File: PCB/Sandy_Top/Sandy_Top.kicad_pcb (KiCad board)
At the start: 2 copper layers, 285 x 37 mm, 64 parts, among them J1 Conn_02x02_Top_Bottom, J2 Conn_02x02_Top_Bottom, J3 Conn_02x02_Top_Bottom

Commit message: キーの間からEXT端子が見えないように移動した
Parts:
- moved EXT_TC3 1.19 mm to (149.6, 21.1)
- moved EXT_TC7 1.19 mm to (280.6, 21.1)
- moved EXT_TC0 1.19 mm to (35.3, 21.1)
- moved EXT_TC2 1.19 mm to (92.5, 21.1)
- moved EXT_TC1 1.19 mm to (73.4, 21.1)
- moved EXT_TC4 1.19 mm to (166.3, 21.0)
- moved EXT_TC6 1.19 mm to (261.6, 21.1)
- moved EXT_TR5 1.19 mm to (54.4, 21.1)
- moved EXT_TR0 1.19 mm to (35.3, 33.0)
- moved EXT_TC5 1.19 mm to (223.5, 21.1)
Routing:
- net Top_col2: track 62.9 -> 61.7 mm
- net Top_col7: track 139.3 -> 140.0 mm
- net Top_col4: track 76.2 -> 75.5 mm

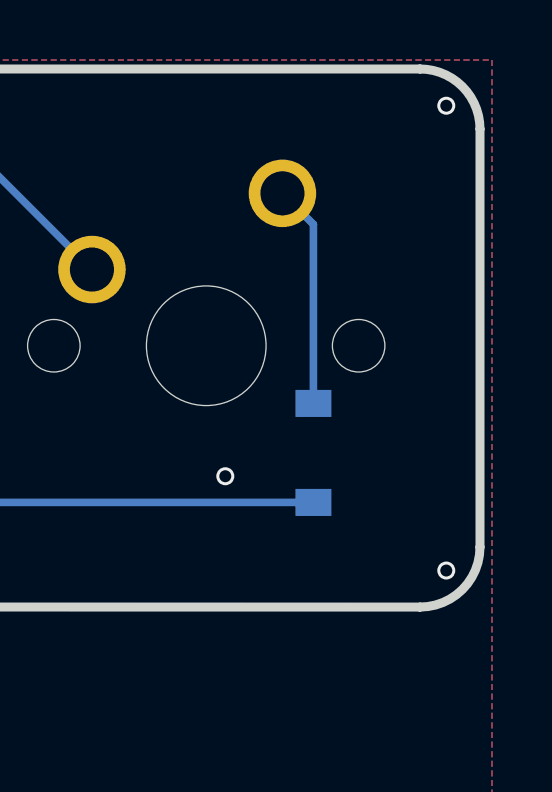
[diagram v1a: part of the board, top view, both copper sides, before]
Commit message: コネクタの接続先がわかるシルクを追加
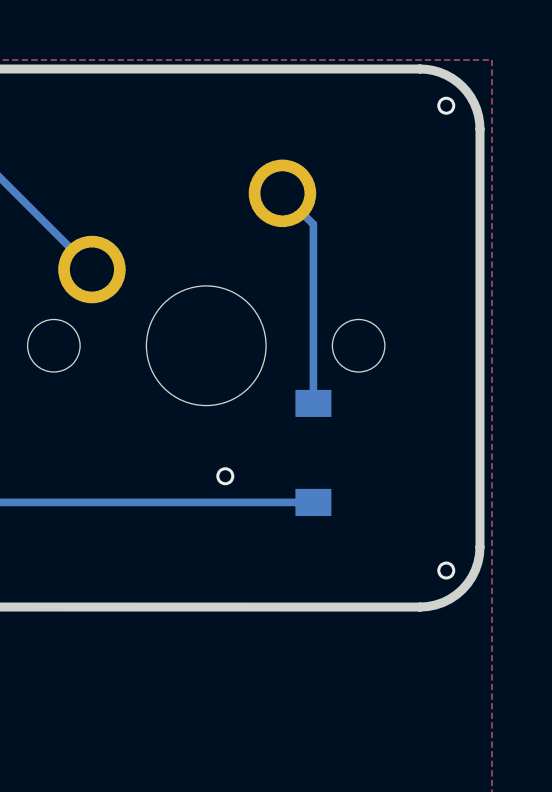
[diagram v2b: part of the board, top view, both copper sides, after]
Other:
- board text added: "Top 1"
- board text added: "Top 2"
- board text added: "Top 3"
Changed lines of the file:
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@@
     (fp_arc (start -140.510786 -0.814254) (mid -141.925 -1.40004) (end -142.510786 -2.814254) (layer "Edge.Cuts") (width 0.3))
     (fp_arc (start -39.470786 -0.82504) (mid -38.056572 -0.239254) (end -37.470786 1.17496) (layer "Edge.Cuts") (width 0.3))
-    (fp_arc (start 142.475 -2.814254) (mid 141.889203 -1.400035) (end 140.475 -0.814254) (layer "Edge.Cuts") (width 0.3))
+    (fp_arc (start 142.475 -2.814254) (mid 141.889197 -1.40007) (end 140.475 -0.814254) (layer "Edge.Cuts") (width 0.3))
     (fp_arc (start -35.470786 18.24996) (mid -36.885 17.664174) (end -37.470786 16.24996) (layer "Edge.Cuts") (width 0.3))
-    (fp_arc (start 140.475 -18.75004) (mid 141.889257 -18.164285) (end 142.475 -16.75004) (layer "Edge.Cuts") (width 0.3))
+    (fp_arc (start 140.475 -18.75004) (mid 141.889222 -18.164279) (end 142.475 -16.75004) (layer "Edge.Cuts") (width 0.3))
     (fp_arc (start -142.525 -16.75004) (mid -141.939214 -18.164254) (end -140.525 -18.75004) (layer "Edge.Cuts") (width 0.3))
     (fp_circle (center -47.625 -14.50004) (end -45.425 -14.50004) (layer "Edge.Cuts") (width 0.15) (fill none))
@@
     (property "Sheetname" "")
     (attr exclude_from_pos_files)
-    (fp_text reference "EXT_TR1" (at 0 1.998) (layer "B.SilkS")
+    (fp_text reference "EXT_TR1" (at -2.111375 -2.286) (layer "B.SilkS")
       (effects (font (size 1 1) (thickness 0.15)) (justify mirror))
     )
@@
     (property "Sheetname" "")
     (attr exclude_from_pos_files)
-    (fp_text reference "EXT_TR6" (at 0 -2.38125) (layer "B.SilkS")
+    (fp_text reference "EXT_TR6" (at 2.19075 -2.286) (layer "B.SilkS")
       (effects (font (size 1 1) (thickness 0.15)) (justify mirror))
     )
@@
     )
   )
+  (gr_text "Top 1" (at 172.26781 31.765905 90) (layer "B.SilkS")
+    (effects (font (size 1.2 1.2) (thickness 0.15)) (justify mirror))
+  )
+  (gr_text "Top 3" (at 153.21781 31.765905 90) (layer "B.SilkS")
+    (effects (font (size 1.2 1.2) (thickness 0.15)) (justify mirror))
+  )
+  (gr_text "Top 2" (at 131.78656 30.57528) (layer "B.SilkS")
+    (effects (font (size 1.2 1.2) (thickness 0.15)) (justify mirror))
+  )
   (gr_text "JLCJLCJLCJLC" (at 290.94931 34.242405) (layer "B.SilkS")

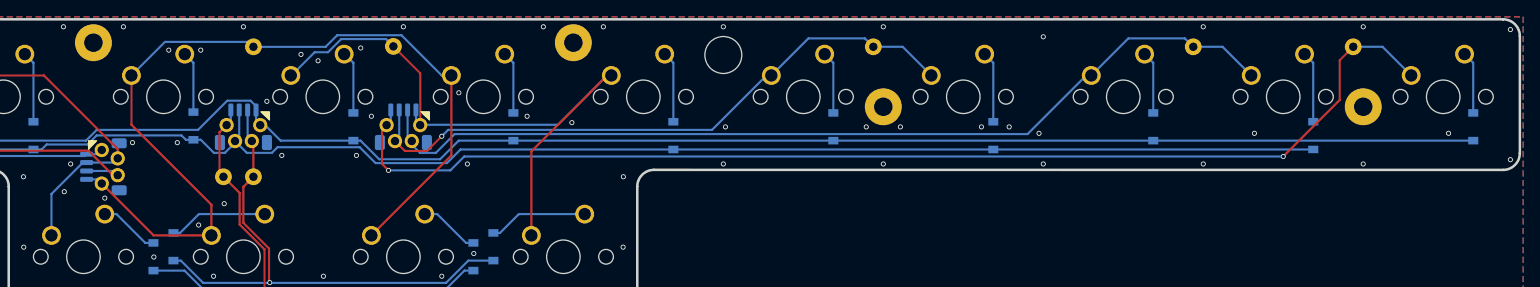
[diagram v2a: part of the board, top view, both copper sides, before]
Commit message: "Back Side"シルク位置調整
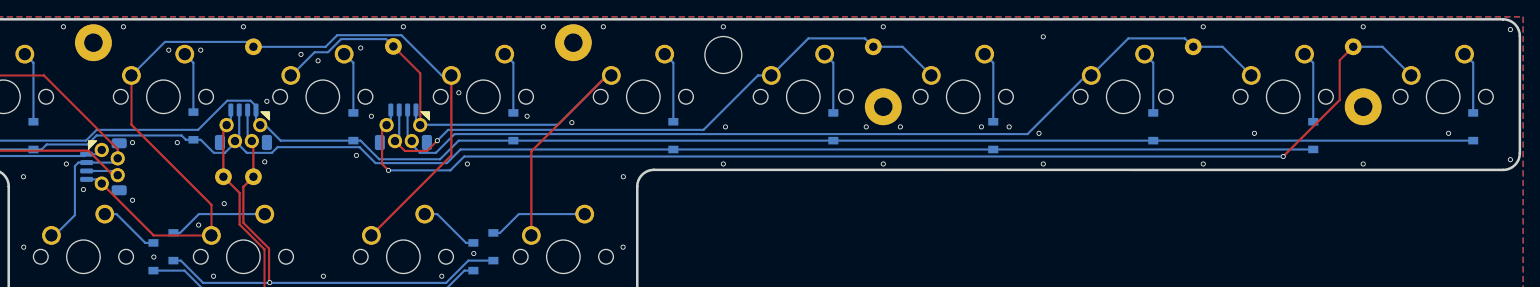
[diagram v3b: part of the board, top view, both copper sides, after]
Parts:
- removed G***: LOGO, Jones.local:Sandy_logo_w15
- renumbered J3 to J1, J1 to J3
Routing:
- net Top_col2: track 61.7 -> 62.2 mm

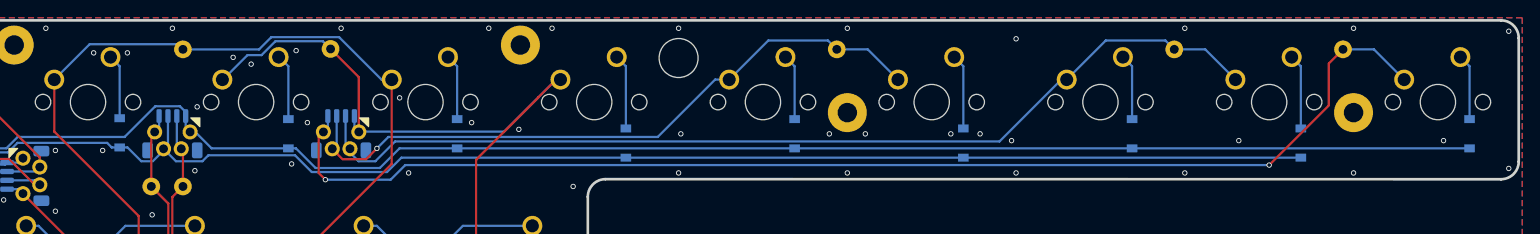
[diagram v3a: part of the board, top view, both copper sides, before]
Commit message: GNDベタ調整
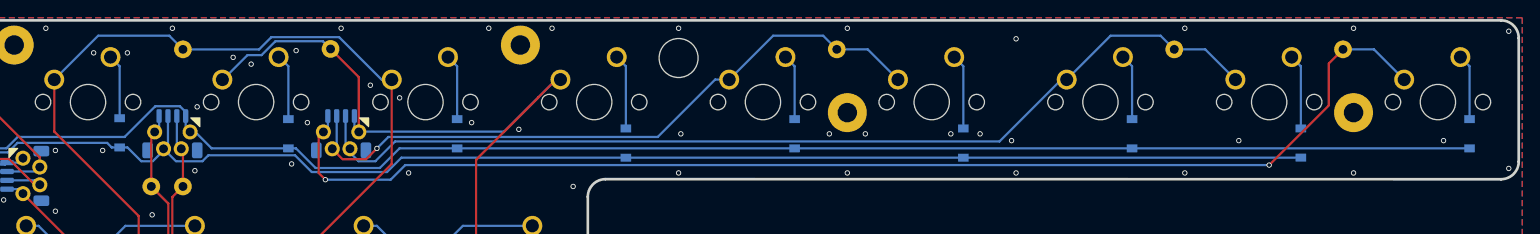
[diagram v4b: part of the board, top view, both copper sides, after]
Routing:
- net Top_col3: track 106.2 -> 107.0 mm
- net Top_GND: vias 78 -> 79
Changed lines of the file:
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@@
     (fp_arc (start -140.510786 -0.814254) (mid -141.925 -1.40004) (end -142.510786 -2.814254) (layer "Edge.Cuts") (width 0.3))
     (fp_arc (start -39.470786 -0.82504) (mid -38.056572 -0.239254) (end -37.470786 1.17496) (layer "Edge.Cuts") (width 0.3))
-    (fp_arc (start 142.475 -2.814254) (mid 141.889203 -1.400035) (end 140.475 -0.814254) (layer "Edge.Cuts") (width 0.3))
+    (fp_arc (start 142.475 -2.814254) (mid 141.889197 -1.40007) (end 140.475 -0.814254) (layer "Edge.Cuts") (width 0.3))
     (fp_arc (start -35.470786 18.24996) (mid -36.885 17.664174) (end -37.470786 16.24996) (layer "Edge.Cuts") (width 0.3))
-    (fp_arc (start 140.475 -18.75004) (mid 141.889257 -18.164285) (end 142.475 -16.75004) (layer "Edge.Cuts") (width 0.3))
+    (fp_arc (start 140.475 -18.75004) (mid 141.889222 -18.164279) (end 142.475 -16.75004) (layer "Edge.Cuts") (width 0.3))
     (fp_arc (start -142.525 -16.75004) (mid -141.939214 -18.164254) (end -140.525 -18.75004) (layer "Edge.Cuts") (width 0.3))
     (fp_circle (center -47.625 -14.50004) (end -45.425 -14.50004) (layer "Edge.Cuts") (width 0.15) (fill none))
@@
   (segment (start 172.069372 24.463405) (end 167.279172 19.673205) (width 0.254) (layer "B.Cu") (net 27))
   (segment (start 129.78656 36.83778) (end 131.08656 36.83778) (width 0.254) (layer "B.Cu") (net 27))
-  (segment (start 135.12031 24.463405) (end 139.11551 20.468205) (width 0.254) (layer "B.Cu") (net 27))
   (segment (start 131.08656 36.83778) (end 131.58656 37.33778) (width 0.254) (layer "B.Cu") (net 27))
   (segment (start 149.65531 21.059655) (end 149.645935 21.05028) (width 0.254) (layer "B.Cu") (net 27))
+  (segment (start 140.07331 19.510405) (end 148.10606 19.510405) (width 0.254) (layer "B.Cu") (net 27))
   (segment (start 173.22031 24.463405) (end 172.069372 24.463405) (width 0.254) (layer "B.Cu") (net 27))
+  (segment (start 148.10606 19.510405) (end 149.645935 21.05028) (width 0.254) (layer "B.Cu") (net 27))
   (segment (start 167.279172 19.673205) (end 159.62726 19.673205) (width 0.254) (layer "B.Cu") (net 27))
   (segment (start 159.62726 19.673205) (end 158.24081 21.059655) (width 0.254) (layer "B.Cu") (net 27))
-  (segment (start 149.06386 20.468205) (end 149.645935 21.05028) (width 0.254) (layer "B.Cu") (net 27))
-  (segment (start 139.11551 20.468205) (end 149.06386 20.468205) (width 0.254) (layer "B.Cu") (net 27))
   (segment (start 158.24081 21.059655) (end 149.65531 21.059655) (width 0.254) (layer "B.Cu") (net 27))
+  (segment (start 135.12031 24.463405) (end 140.07331 19.510405) (width 0.254) (layer "B.Cu") (net 27))
   (segment (start 169.50531 24.19403) (end 166.314685 21.003405) (width 0.254) (layer "F.Cu") (net 28))
   (segment (start 169.50531 30.37528) (end 169.50531 24.19403) (width 0.254) (layer "F.Cu") (net 28))
@@
   (segment (start 167.68551 33.45548) (end 170.324236 33.45548) (width 0.254) (layer "F.Cu") (net 29))
   (via (at 171.545498 32.234218) (size 0.6) (drill 0.4) (layers "F.Cu" "B.Cu") (net 29))
+  (segment (start 216.27331 19.510405) (end 211.32031 24.463405) (width 0.254) (layer "B.Cu") (net 29))
   (segment (start 172.839311 30.940405) (end 171.545498 32.234218) (width 0.254) (layer "B.Cu") (net 29))
   (segment (start 209.72932 24.463405) (end 203.25232 30.940405) (width 0.254) (layer "B.Cu") (net 29))
+  (segment (start 221.92481 19.510405) (end 216.27331 19.510405) (width 0.254) (layer "B.Cu") (net 29))
   (segment (start 167.00531 31.77528) (end 167.00531 28.57528) (width 0.254) (layer "B.Cu") (net 29))
   (segment (start 203.25232 30.940405) (end 172.839311 30.940405) (width 0.254) (layer "B.Cu") (net 29))
   (segment (start 211.32031 24.463405) (end 209.72932 24.463405) (width 0.254) (layer "B.Cu") (net 29))
   (segment (start 166.50531 32.27528) (end 167.00531 31.77528) (width 0.254) (layer "B.Cu") (net 29))
-  (segment (start 222.464685 20.05028) (end 215.733435 20.05028) (width 0.254) (layer "B.Cu") (net 29))
   (segment (start 223.464685 21.05028) (end 226.957185 21.05028) (width 0.254) (layer "B.Cu") (net 29))
-  (segment (start 215.733435 20.05028) (end 211.32031 24.463405) (width 0.254) (layer "B.Cu") (net 29))
   (segment (start 226.957185 21.05028) (end 230.37031 24.463405) (width 0.254) (layer "B.Cu") (net 29))
-  (segment (start 223.464685 21.05028) (end 222.464685 20.05028) (width 0.254) (layer "B.Cu") (net 29))
+  (segment (start 223.464685 21.05028) (end 221.92481 19.510405) (width 0.254) (layer "B.Cu") (net 29))
   (segment (start 168.50531 32.27528) (end 168.00531 31.77528) (width 0.254) (layer "B.Cu") (net 30))
   (segment (start 173.604635 31.44508) (end 171.369235 33.68048) (width 0.254) (layer "B.Cu") (net 30))
   (segment (start 169.483385 33.68048) (end 168.50531 32.702405) (width 0.254) (layer "B.Cu") (net 30))
   (segment (start 171.369235 33.68048) (end 169.483385 33.68048) (width 0.254) (layer "B.Cu") (net 30))
+  (segment (start 260.02481 19.510405) (end 254.37331 19.510405) (width 0.254) (layer "B.Cu") (net 30))
+  (segment (start 261.564685 21.05028) (end 260.02481 19.510405) (width 0.254) (layer "B.Cu") (net 30))
+  (segment (start 254.37331 19.510405) (end 249.42031 24.463405) (width 0.254) (layer "B.Cu") (net 30))
   (segment (start 248.81706 24.463405) (end 241.835385 31.44508) (width 0.254) (layer "B.Cu") (net 30))
   (segment (start 168.00531 31.77528) (end 168.00531 28.57528) (width 0.254) (layer "B.Cu") (net 30))
   (segment (start 261.564685 21.05028) (end 265.057185 21.05028) (width 0.254) (layer "B.Cu") (net 30))
-  (segment (start 260.564685 20.05028) (end 253.833435 20.05028) (width 0.254) (layer "B.Cu") (net 30))
-  (segment (start 261.564685 21.05028) (end 260.564685 20.05028) (width 0.254) (layer "B.Cu") (net 30))
   (segment (start 265.057185 21.05028) (end 268.47031 24.463405) (width 0.254) (layer "B.Cu") (net 30))
   (segment (start 249.42031 24.463405) (end 248.81706 24.463405) (width 0.254) (layer "B.Cu") (net 30))
   (segment (start 241.835385 31.44508) (end 173.604635 31.44508) (width 0.254) (layer "B.Cu") (net 30))
   (segment (start 168.50531 32.702405) (end 168.50531 32.27528) (width 0.254) (layer "B.Cu") (net 30))
-  (segment (start 253.833435 20.05028) (end 249.42031 24.463405) (width 0.254) (layer "B.Cu") (net 30))
   (segment (start 164.96531 30.91528) (end 164.96531 35.004405) (width 0.254) (layer "F.Cu") (net 31))
   (segment (start 279.01131 27.384405) (end 272.28031 34.115405) (width 0.254) (layer "F.Cu") (net 31))
@@
   (via (at 16.62931 34.496405) (size 0.6) (drill 0.4) (layers "F.Cu" "B.Cu") (free) (net 32))
   (via (at 157.98031 53.197155) (size 0.6) (drill 0.4) (layers "F.Cu" "B.Cu") (free) (net 32))
+  (via (at 170.80731 25.098405) (size 0.6) (drill 0.4) (layers "F.Cu" "B.Cu") (free) (net 32))
   (via (at 139.56531 21.447155) (size 0.6) (drill 0.4) (layers "F.Cu" "B.Cu") (free) (net 32))
   (via (at 187.57131 30.083155) (size 0.6) (drill 0.4) (layers "F.Cu" "B.Cu") (free) (net 32))
